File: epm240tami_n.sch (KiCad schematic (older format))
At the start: 25 parts, among them CON1 AB2_POWER_BARREL, P1 CONN_01X02, P2 CONN_01X02, P3 CONN_01X02, P4 CONN_02X22, P5 CONN_02X22, P6 JTAG, P7 CONN_01X07, U1 EPM240T100C5N, U2 AMS1117-3.3V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

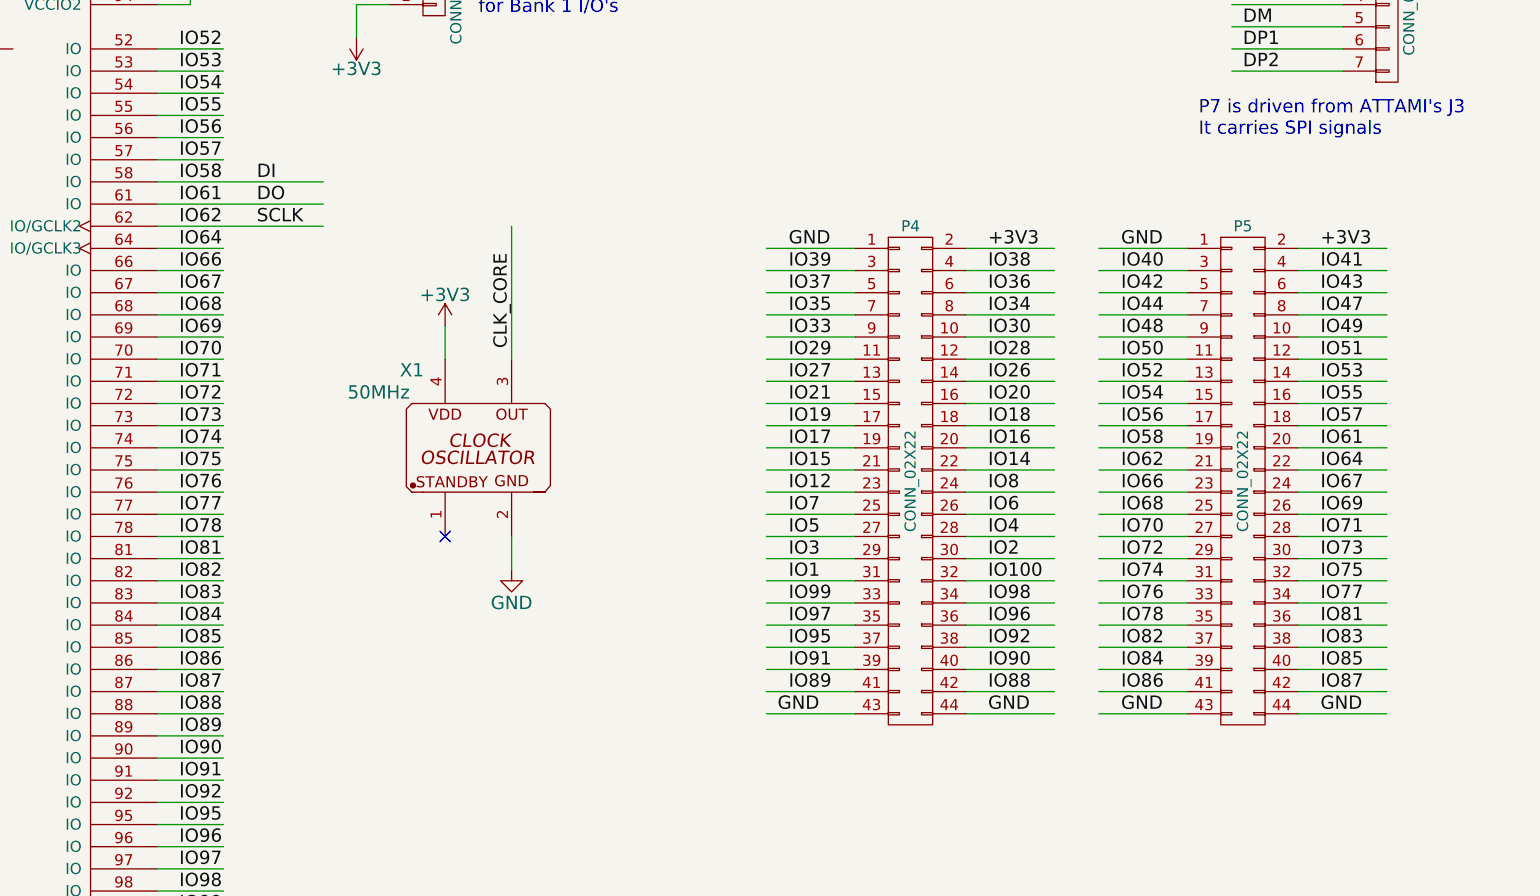
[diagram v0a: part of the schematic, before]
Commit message: Updated schematic and moved DI/DO around to reduce routing due to new placement. Added PDF file
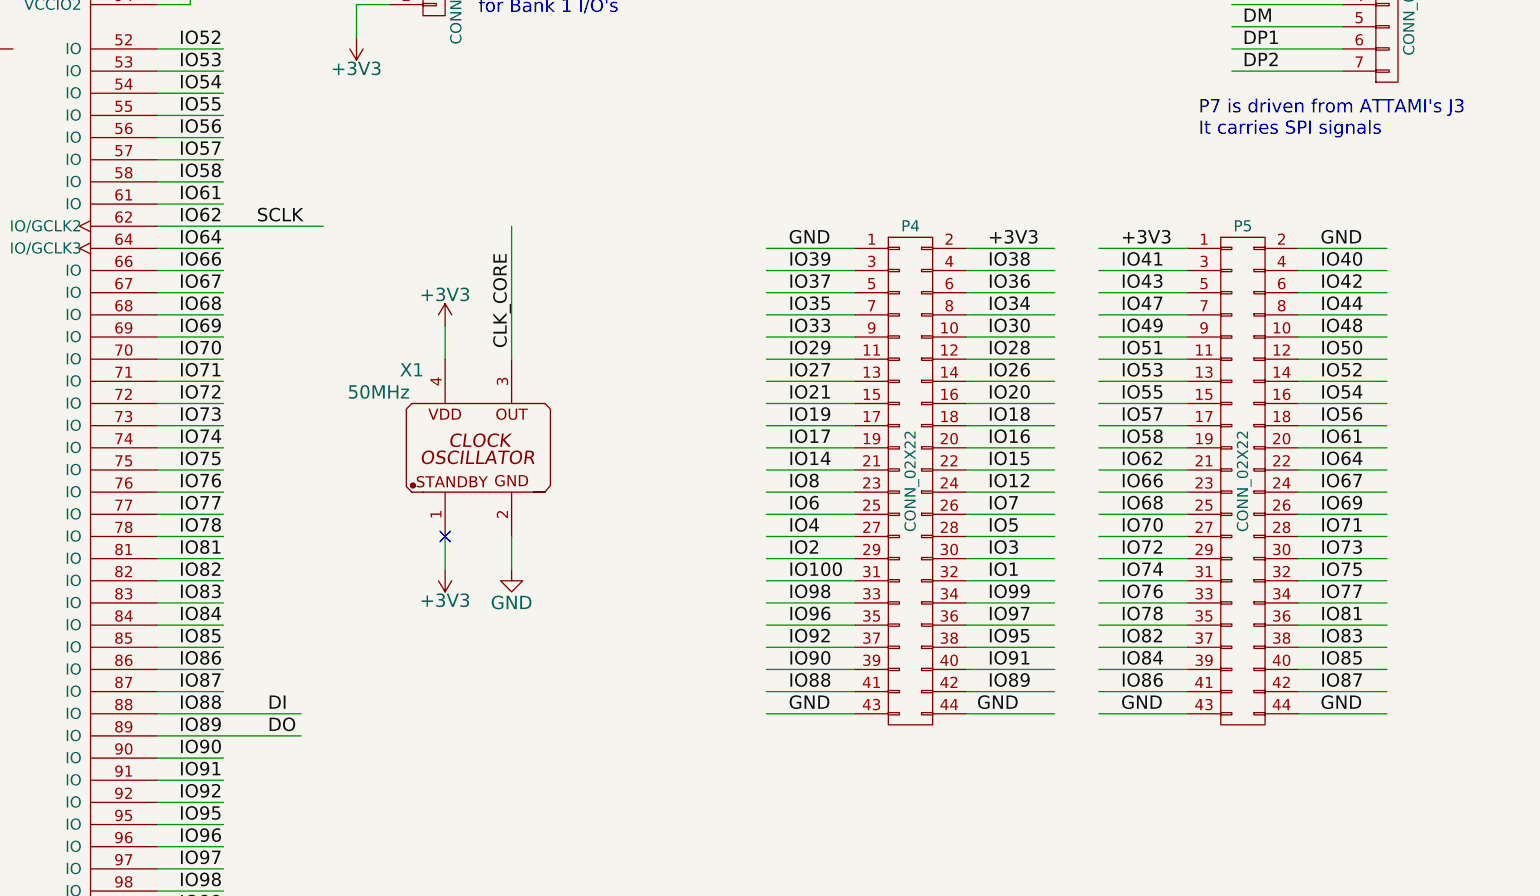
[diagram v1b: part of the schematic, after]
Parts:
- P1, P3: footprint (none) -> Pin_Headers:Pin_Header_Straight_1x02
- X1: footprint Oscillator-Modules:OSCILLATOR_KXO-200 -> Crystals_Oscillators_SMD:crystal_HXO-3
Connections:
- wire segments 264 -> 265
